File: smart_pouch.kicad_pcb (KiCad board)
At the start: 2 copper layers, 92 parts, among them CN1 B3B-PH-K-S, J1 XH-2P-SMD, J2 2.54-3P-LT, J3 SIM_Card, Q2 PMV20XNER, Q3 2N7002, SW1 SW_Push, U1 nRF52840, U10 BWU.FL-IPEX1, U11 HX PZ1.27-2x5P TP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

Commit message: gpt-footprint-bom-run
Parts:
- U9: value SM04B-SRSS-TB -> XH-4A; footprint easyeda2kicad:CONN-SMD_4P-P1.00_SM04B-SRSS-TB-LF-SN -> easyeda2kicad:CONN-TH_B4B-XH-A-LF-SN
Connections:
- C29 pad 2: +1V8 -> /VTref_9151
- R3 pad 1: Net-(J3-CLK) -> /SIM_CLK
- R4 pad 1: Net-(J3-I/O) -> /SIM_IO
- U2 pad 65: +1V8 -> /VTref_9151
- U2 pad 75: /VTref_9151 -> unconnected-(U2-P0.15-Pad75)

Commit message: Initial PCB commit
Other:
- copper layers 2 -> 4
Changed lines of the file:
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@@
 	(layers
 		(0 "F.Cu" signal)
+		(4 "In1.Cu" signal)
+		(6 "In2.Cu" signal)
 		(2 "B.Cu" signal)
 		(9 "F.Adhes" user "F.Adhesive")
@@
 	)
 	(setup
+		(stackup
+			(layer "F.SilkS"
+				(type "Top Silk Screen")
+			)
+			(layer "F.Paste"
+				(type "Top Solder Paste")
+			)
+			(layer "F.Mask"
+				(type "Top Solder Mask")
+				(thickness 0.01)
+			)
+			(layer "F.Cu"
+				(type "copper")
+				(thickness 0.035)
+			)
+			(layer "dielectric 1"
+				(type "prepreg")
+				(color "FR4 natural")
+				(thickness 0.0994)
+				(material "3313")
+				(epsilon_r 4.1)
+				(loss_tangent 0.02)
+			)
+			(layer "In1.Cu"
+				(type "copper")
+				(thickness 0.0152)
+			)
+			(layer "dielectric 2"
+				(type "core")
+				(color "FR4 natural")
+				(thickness 1.265)
+				(material "FR4")
+				(epsilon_r 4.6)
+				(loss_tangent 0.02)
+			)
+			(layer "In2.Cu"
+				(type "copper")
+				(thickness 0.0152)
+			)
+			(layer "dielectric 3"
+				(type "prepreg")
+				(color "FR4 natural")
+				(thickness 0.0994)
+				(material "3313")
+				(epsilon_r 4.1)
+				(loss_tangent 0.02)
+			)
+			(layer "B.Cu"
+				(type "copper")
+				(thickness 0.035)
+			)
+			(layer "B.Mask"
+				(type "Bottom Solder Mask")
+				(thickness 0.01)
+			)
+			(layer "B.Paste"
+				(type "Bottom Solder Paste")
+			)
+			(layer "B.SilkS"
+				(type "Bottom Silk Screen")
+			)
+			(copper_finish "ENIG")
+			(dielectric_constraints yes)
+		)
 		(pad_to_mask_clearance 0)
 		(allow_soldermask_bridges_in_footprints no)

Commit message: pcb basic layout
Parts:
- removed C1, C30: 100nF, Capacitor_SMD:C_0402_1005Metric
- removed D3: SP3012-04UTG, easyeda2kicad:UDFN-10_L2.5-W1.0-P0.50-BL
- removed J3: SIM_Card, easyeda2kicad:SIM-SMD_SMN-303
- removed R3, R4: 10k, Resistor_SMD:R_0402_1005Metric
- added C14: 100nF, Capacitor_SMD:C_0402_1005Metric, F.Cu at (154.0, 102.0)
- added C3: 100nF, Capacitor_SMD:C_0402_1005Metric, F.Cu at (107.0, 70.8)
- added C34: 12pF, Capacitor_SMD:C_0402_1005Metric, F.Cu at (137.5, 60.3)
- added C36: 100nF, Capacitor_SMD:C_0402_1005Metric, F.Cu at (67.5, 108.6)
- added C37: 100nF, Capacitor_SMD:C_0402_1005Metric, F.Cu at (64.0, 107.6)
- added C4: 12pF, Capacitor_SMD:C_0402_1005Metric, F.Cu at (142.0, 72.3)
- added Card1: SMN-303, easyeda2kicad:SIM-SMD_SMN-303, F.Cu at (65.5, 120.1)
- added R10: 39R, Resistor_SMD:R_2512_6332Metric, B.Cu at (143.9, 106.2)
- added R11: 150R, Resistor_SMD:R_0402_1005Metric, B.Cu at (133.3, 90.6)
- added R12: 10k, Resistor_SMD:R_0402_1005Metric, B.Cu at (131.7, 85.5)
- added R13: 560k, Resistor_SMD:R_0402_1005Metric, F.Cu at (157.0, 97.0)
- added R14: 2.2M, Resistor_SMD:R_0402_1005Metric, F.Cu at (152.5, 97.0)
- added R15: 100k, Resistor_SMD:R_0402_1005Metric, F.Cu at (164.0, 89.0)
- added R16: 10k, Resistor_SMD:R_0402_1005Metric, F.Cu at (166.2, 78.0)
- added R17: 10k, Resistor_SMD:R_0402_1005Metric, F.Cu at (159.5, 79.0)
- added R23: 18k, Resistor_SMD:R_0402_1005Metric, F.Cu at (174.5, 109.0)
- added R29: 100k, Resistor_SMD:R_0402_1005Metric, F.Cu at (179.0, 99.0)
- added R31: 10k, Resistor_SMD:R_0402_1005Metric, F.Cu at (60.0, 110.1)
- added R7: 39R, Resistor_SMD:R_2512_6332Metric, B.Cu at (143.9, 91.5)
- added R8: 39R, Resistor_SMD:R_2512_6332Metric, B.Cu at (143.9, 96.4)
- added R9: 39R, Resistor_SMD:R_2512_6332Metric, B.Cu at (143.9, 101.3)
- added TP1: TestPoint, TestPoint:TestPoint_Pad_1.0x1.0mm, F.Cu at (67.5, 72.5)
- added TP2: TestPoint, TestPoint:TestPoint_Pad_1.0x1.0mm, F.Cu at (70.5, 72.5)
- added TP3: TestPoint, TestPoint:TestPoint_Pad_1.0x1.0mm, F.Cu at (73.6, 72.5)
- added Y2: 32.768kHz, Crystal:Crystal_SMD_3215-2Pin_3.2x1.5mm, F.Cu at (143.4, 64.8)
- CN1: value B3B-PH-K-S -> JST 1x3 Battery P=1.27mm
- D1, D10, D11, D4, D6, D7, D8, D9, R28, R5, R6: moved to B.Cu
- D5: value PRTR5V0U2X -> PRTR5V0U2X ESD
- J1: value XH-2P-SMD -> Solenoid XH-2P-SMD
- J2: value 2.54-3P-LT -> 2.54-3P-LT Piezo
- LED1: value 19-237/R6GHBHC-A01/2T -> Power RGB; moved to B.Cu
- LED2: value 19-237/R6GHBHC-A01/2T -> USER LED; moved to B.Cu
- U11: value HX PZ1.27-2x5P TP -> 9151 SWD P=1.27mm 2x5P
- U14: value HX PZ1.27-2x5P TP -> 52840 SWD P=1.27mm 2x5P
- U8: value SEN0348_CONN -> JST P=1mm 01x06
- U9: value XH-4A -> XH-4A UART 9151
- USB1: value TYPE-C 16PIN 2MD -> TYPE-C 16P
- moved C_ANT2 108.9 mm to (63.0, 83.0)
- moved U7 108.1 mm to (61.0, 62.0), turned to 180 degrees
- moved R30 105.2 mm to (67.0, 87.5)
- moved C25 104.8 mm to (61.0, 75.0)
- moved C_ANT1 102.0 mm to (70.0, 82.5)
- moved C26 97.7 mm to (68.0, 78.0)
- moved Q2 89.1 mm to (79.5, 89.5)
- moved U10 85.2 mm to (76.7, 61.5)
- moved U6 85.2 mm to (72.2, 61.5)
- moved USB1 77.8 mm to (214.4, 77.5), turned to 90 degrees
- moved LED1 75.2 mm to (214.0, 67.0), turned to 180 degrees
- moved C33 70.7 mm to (109.0, 57.8)
- moved L2 67.2 mm to (192.0, 91.3)
- moved L3 67.2 mm to (192.0, 96.7)
- moved R27 66.9 mm to (108.5, 67.3)
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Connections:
- U2 pad 26: unconnected-(U2-SIM_DET-Pad26) -> /SIM_CD
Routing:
- added copper zone on F.Cu, net GND
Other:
- board outline added: 169 x 79.5 mm

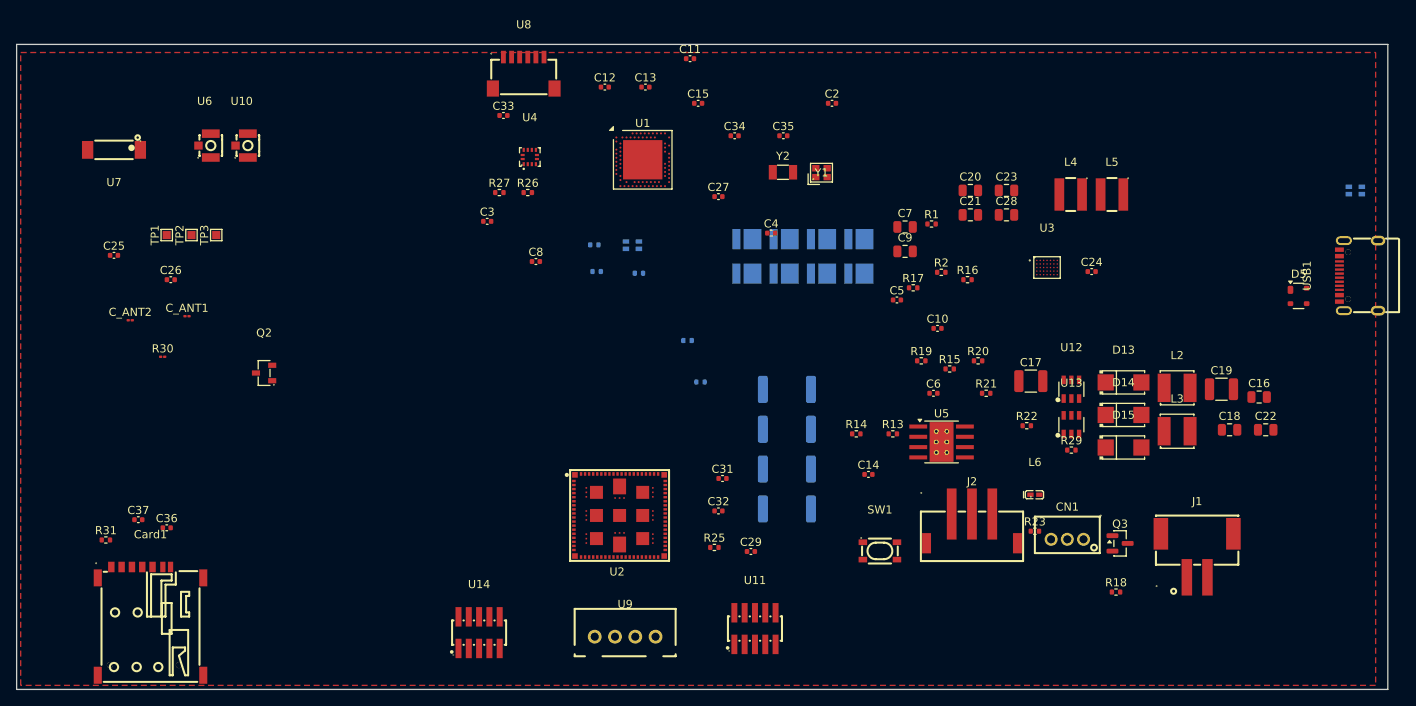
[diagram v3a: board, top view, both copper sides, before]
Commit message: replace npm13100 package
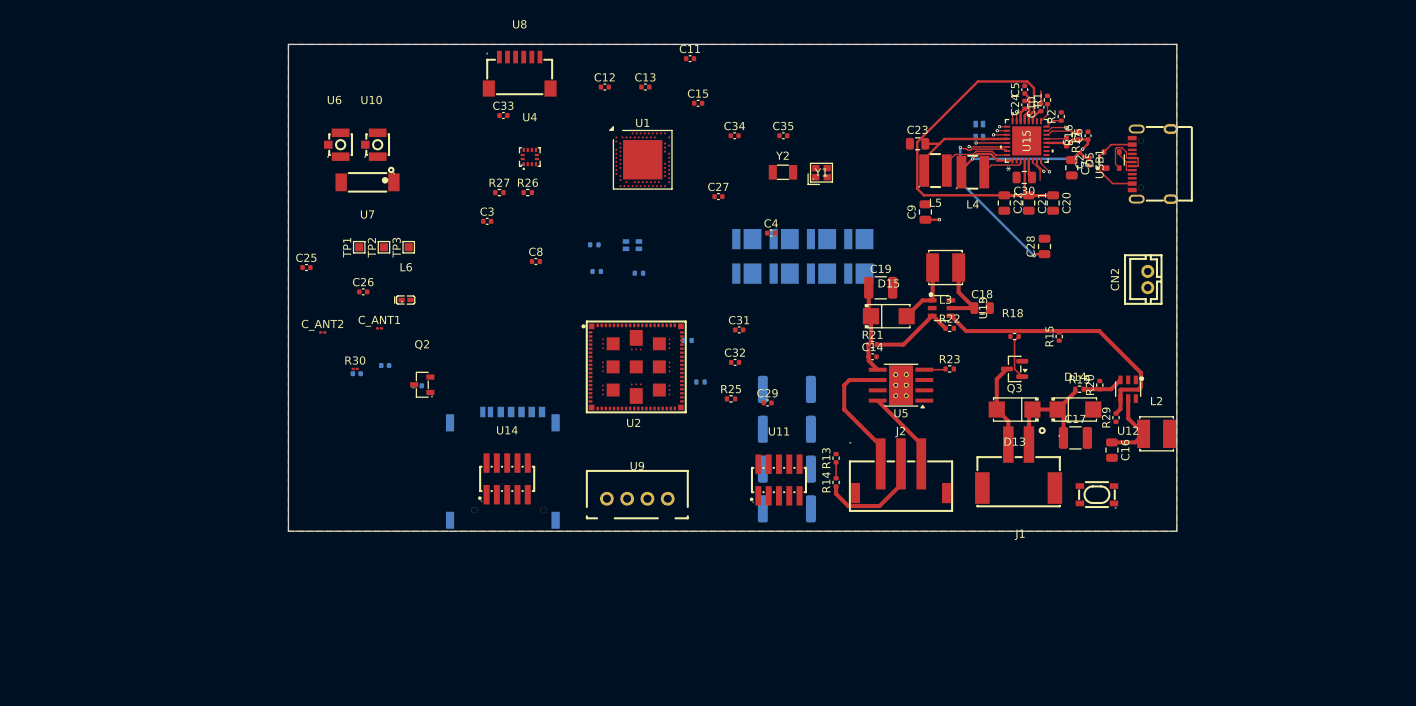
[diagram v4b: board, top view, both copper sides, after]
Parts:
- removed CN1: JST 1x3 Battery P=1.27mm, easyeda2kicad:CONN-TH_B3B-PH-K-S
- removed U3: NPM1300, easyeda2kicad:BGA-35_L3.1-W2.4-R5-C7-P0.42_NPM1300-CAAA-R
- added C30: 10uF, Capacitor_SMD:C_0805_2012Metric, F.Cu at (173.2, 65.4)
- added CN2: B2B-PH-K-S, easyeda2kicad:CONN-TH_B2B-PH-K-S, F.Cu at (188.4, 78.0)
- added U15: NPM1300-QEAA-R7, footprints2:QFN32_5X5_NOR, F.Cu at (173.5, 60.9)
- C36, C37, Card1, R31: moved to B.Cu
- moved L6 81.1 mm to (97.0, 80.5)
- moved Card1 47.4 mm to (108.9, 101.0), turned to 180 degrees
- moved LED1 46.9 mm to (167.7, 59.6), turned to 90 degrees
- moved C19 43.8 mm to (155.5, 79.0)
- moved R31 42.9 mm to (98.4, 91.1), turned to 180 degrees
- moved C22 42.7 mm to (170.7, 68.5), turned to -90 degrees
- moved C6 37.0 mm to (181.1, 60.2), turned to 90 degrees
- moved C37 35.9 mm to (94.4, 88.6), turned to 180 degrees
- moved L3 34.9 mm to (163.5, 76.5), turned to 180 degrees
- moved C18 34.0 mm to (168.0, 81.5)
- moved R18 33.9 mm to (172.0, 85.0)
- moved D15 33.1 mm to (156.5, 82.5)
- moved C2 32.5 mm to (181.2, 63.5), turned to 90 degrees
- moved U7 31.5 mm to (92.2, 66.0)
- moved C5 30.3 mm to (173.2, 54.6), turned to 90 degrees
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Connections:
- net Net-(J2-Pin_1) renamed /+
- net Net-(J2-Pin_2) renamed /FB
- net Net-(J2-Pin_3) renamed /-
- C7 pad 1: GND -> +1V8
- C7 pad 2: +1V8 -> GND
- LED1 pad 2: Net-(LED1-G-) -> Net-(LED1-B-)
- R16 pad 1: /NPM_SCL -> +1V8
- R16 pad 2: +1V8 -> Net-(U15-SCL)
- U1 pad AC11: /NPM_SCL -> +1V8
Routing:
- net /ALARM_LS: track 0.00 -> 58.4 mm, vias 0 -> 2
- net /VSYS: track 0.00 -> 55.6 mm
- net +1V8: track 0.00 -> 32.4 mm, vias 0 -> 2
- net +3.3V: track 0.00 -> 16.7 mm
- net /+: track 0.00 -> 16.0 mm
- net /VBUS: track 0.00 -> 14.9 mm
- net +12V: track 0.00 -> 14.8 mm
- net /FB: track 0.00 -> 13.2 mm
- net +15V: track 0.00 -> 10.8 mm
- net Net-(U13-FB): track 0.00 -> 10.6 mm
- net Net-(D13-A): track 0.00 -> 10.4 mm
- net /-: track 0.00 -> 10.0 mm
- net Net-(U12-IN): track 0.00 -> 9.47 mm
- net Net-(U15-VOUT2): track 0.00 -> 9.16 mm
- net Net-(U13-IN): track 0.00 -> 8.71 mm
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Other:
- board size 169 x 79.5 mm -> 109.5 x 60 mm
- board text added: "U3 WLCSP via-in-pad vias must be filled and plated over. ENIG required."

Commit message: poop
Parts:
- removed C10: 2.2uF, Capacitor_SMD:C_0402_1005Metric
- removed C11: 100pF, Capacitor_SMD:C_0402_1005Metric
- removed C12, C2, C24, C5: 1uF, Capacitor_SMD:C_0402_1005Metric
- removed C13, C14, C29, C3, C31, C32, C33, C36, C37, C6, C8: 100nF, Capacitor_SMD:C_0402_1005Metric
- removed C15: 4.7uF, Capacitor_SMD:C_0402_1005Metric
- removed C16, C18, C20, C21, C22, C23, C30, C7: 10uF, Capacitor_SMD:C_0805_2012Metric
- removed C17, C19: 22u 25V, Capacitor_SMD:C_1210_3225Metric
- removed C25: 0.5pF, Capacitor_SMD:C_0402_1005Metric
- removed C26: 0.8pF, Capacitor_SMD:C_0402_1005Metric
- removed C27, C34, C35, C4: 12pF, Capacitor_SMD:C_0402_1005Metric
- removed C28, C9: 1uF, Capacitor_SMD:C_0805_2012Metric
- removed CN2: B2B-PH-K-S, easyeda2kicad:CONN-TH_B2B-PH-K-S
- removed C_ANT1, C_ANT2: DNP, Capacitor_SMD:C_01005_0402Metric
- removed Card1: SMN-303, easyeda2kicad:SIM-SMD_SMN-303
- removed D1, D10, D11, D4, D6, D7, D8, D9: LED, easyeda2kicad:LED-SMD_L3.0-W3.0_XL-3030UWC-1W-3V
- removed D13, D14, D15: SS34_C8678, easyeda2kicad:SMA_L4.3-W2.6-LS5.2-RD
- removed D5: PRTR5V0U2X ESD, Package_TO_SOT_SMD:SOT-143
- removed J1: Solenoid XH-2P-SMD, easyeda2kicad:CONN-SMD_2P-P2.54_XH2.54-2AB
- removed J2: 2.54-3P-LT Piezo, easyeda2kicad:CONN-SMD_2.54-3P-LT
- removed L2, L3: 10uH, easyeda2kicad:IND-SMD_L4.0-W4.0
- removed L4, L5: 2.2uH, easyeda2kicad:IND-SMD_L4.0-W4.0_NRS4018T
- removed L6: 4.7nH, easyeda2kicad:L0402-R-RD
- removed LED1: Power RGB, easyeda2kicad:LED-ARRAY-SMD_4P-L1.6-W1.6-BL_1
- removed LED2: USER LED, easyeda2kicad:LED-ARRAY-SMD_4P-L1.6-W1.6-BL_1
- removed Q2: PMV20XNER, easyeda2kicad:SOT-23-3_L2.9-W1.3-P1.90-LS2.4-BR
- removed Q3: 2N7002, Package_TO_SOT_SMD:SOT-23
- removed R1: 47k, Resistor_SMD:R_0402_1005Metric
- removed R10, R7, R8, R9: 39R, Resistor_SMD:R_2512_6332Metric
- removed R11: 150R, Resistor_SMD:R_0402_1005Metric
- removed R12, R16, R17, R20, R22, R31: 10k, Resistor_SMD:R_0402_1005Metric
- removed R13: 560k, Resistor_SMD:R_0402_1005Metric
- removed R14: 2.2M, Resistor_SMD:R_0402_1005Metric
- removed R15, R25, R29: 100k, Resistor_SMD:R_0402_1005Metric
- removed R18: 100R, Resistor_SMD:R_0402_1005Metric
- removed R19: 191k, Resistor_SMD:R_0402_1005Metric
- removed R2: 330k, Resistor_SMD:R_0402_1005Metric
- removed R21: 240k, Resistor_SMD:R_0402_1005Metric
- removed R23: 18k, Resistor_SMD:R_0402_1005Metric
- removed R26, R27: 4.7k, Resistor_SMD:R_0402_1005Metric
- removed R28, R5, R6: 330, Resistor_SMD:R_0402_1005Metric
- removed R30: 0R, Resistor_SMD:R_01005_0402Metric
- removed SW1: SW_Push, easyeda2kicad:KEY-SMD_4P-L4.2-W3.2-P2.20-LS4.6
- removed TP1, TP2, TP3: TestPoint, TestPoint:TestPoint_Pad_1.0x1.0mm
- removed U1: nRF52840, Package_DFN_QFN:Nordic_AQFN-73-1EP_7x7mm_P0.5mm
- removed U10, U6: BWU.FL-IPEX1, easyeda2kicad:IPEX-SMD_BWIPX-1-001E
- removed U11: 9151 SWD P=1.27mm 2x5P, easyeda2kicad:HDR-SMD_10P-P1.27-V-M-R2-C5-LS5.5_1
- removed U12, U13: MT3608, easyeda2kicad:SOT-23-6_L2.9-W1.6-P0.95-LS2.8-BL
- removed U14: 52840 SWD P=1.27mm 2x5P, easyeda2kicad:HDR-SMD_10P-P1.27-V-M-R2-C5-LS5.5_1
- removed U15: NPM1300-QEAA-R7, footprints2:QFN32_5X5_NOR
- removed U2: NRF9151-LACA-R7, easyeda2kicad:LGA-113_L12.1-W11.1_NRF9151-LACA-R7
- removed U4: BMA400, easyeda2kicad:LGA-12_L2.0-W2.0-P0.50-BL
- removed U5: DRV8871DDA, Package_SO:Texas_HTSOP-8-1EP_3.9x4.9mm_P1.27mm_EP2.95x4.9mm_Mask2.4x3.1mm_ThermalVias
- removed U7: AN6520-245, easyeda2kicad:ANT-SMD_L6.5-W2.0
- removed U8: JST P=1mm 01x06, easyeda2kicad:CONN-SMD_SM06B-SRSS-TB-LF-SN
- removed U9: XH-4A UART 9151, easyeda2kicad:CONN-TH_B4B-XH-A-LF-SN
- removed USB1: TYPE-C 16P, easyeda2kicad:USB-C-SMD_TYPE-C-16PIN-2MD-073
- removed Y1: 32MHz, easyeda2kicad:CRYSTAL-SMD_4P-L2.0-W1.6-BL
- removed Y2: 32.768kHz, Crystal:Crystal_SMD_3215-2Pin_3.2x1.5mm
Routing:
- net /ALARM_LS: track 58.4 -> 0.00 mm, vias 2 -> 0
- net /VSYS: track 55.6 -> 0.00 mm
- net +1V8: track 32.4 -> 0.00 mm, vias 2 -> 0
- net +3.3V: track 16.7 -> 0.00 mm
- net /+: track 16.0 -> 0.00 mm
- net /VBUS: track 14.9 -> 0.00 mm
- net +12V: track 14.8 -> 0.00 mm
- net /FB: track 13.2 -> 0.00 mm
- net +15V: track 10.8 -> 0.00 mm
- net Net-(U13-FB): track 10.6 -> 0.00 mm
- net Net-(D13-A): track 10.4 -> 0.00 mm
- net /-: track 10.0 -> 0.00 mm
- net Net-(U12-IN): track 9.47 -> 0.00 mm
- net Net-(U15-VOUT2): track 9.16 -> 0.00 mm
- net Net-(U13-IN): track 8.71 -> 0.00 mm
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- removed copper zone on F.Cu, net GND
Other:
- board outline removed
- board text removed: "U3 WLCSP via-in-pad vias must be filled and plated over. ENIG required."
